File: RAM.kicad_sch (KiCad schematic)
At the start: 8 parts, among them U2 TXB0108DQSR, U3 TXB0108DQSR, U4 TXB0108DQSR, U5 74LVC1G04, U6 TXB0108DQSR, U7 AS6C1616, U8 TXB0108DQSR

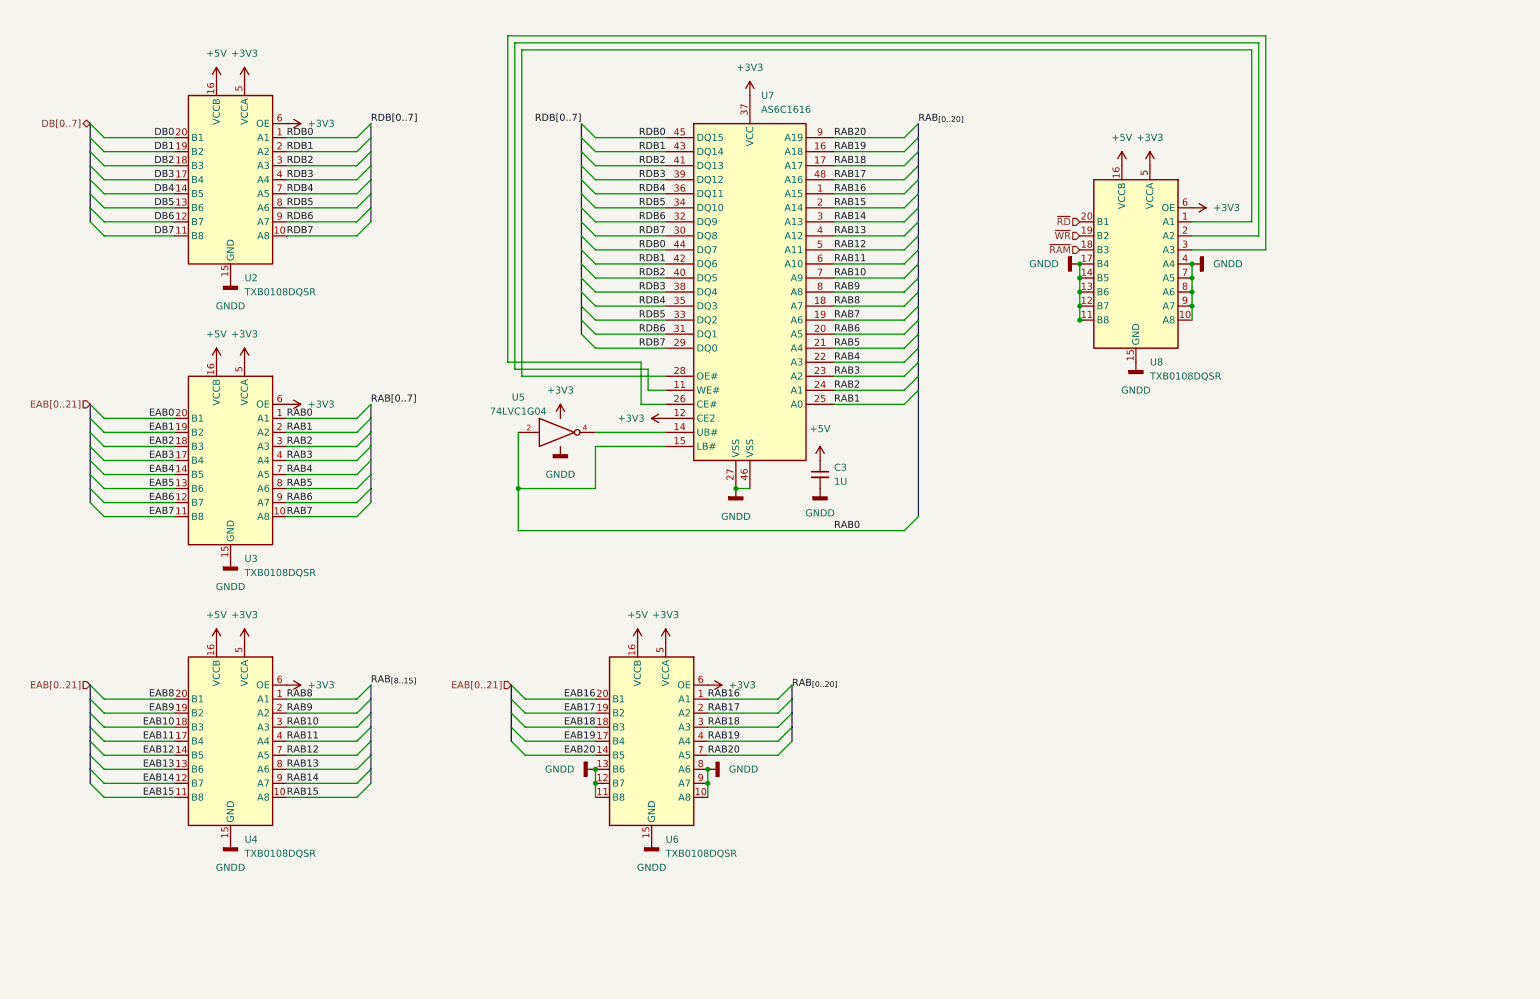
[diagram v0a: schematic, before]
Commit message: final hardware revision
final update to the hardware:
- removed flash
- added battery backup switch-over
- increased ram to 4MB
- added ramboot/netboot option by using reads to write-only ports to trigger/toggle
- fixed a logic bug i should have caught in writes to the mapper registers (using bits 14&15 instead of 1&0)
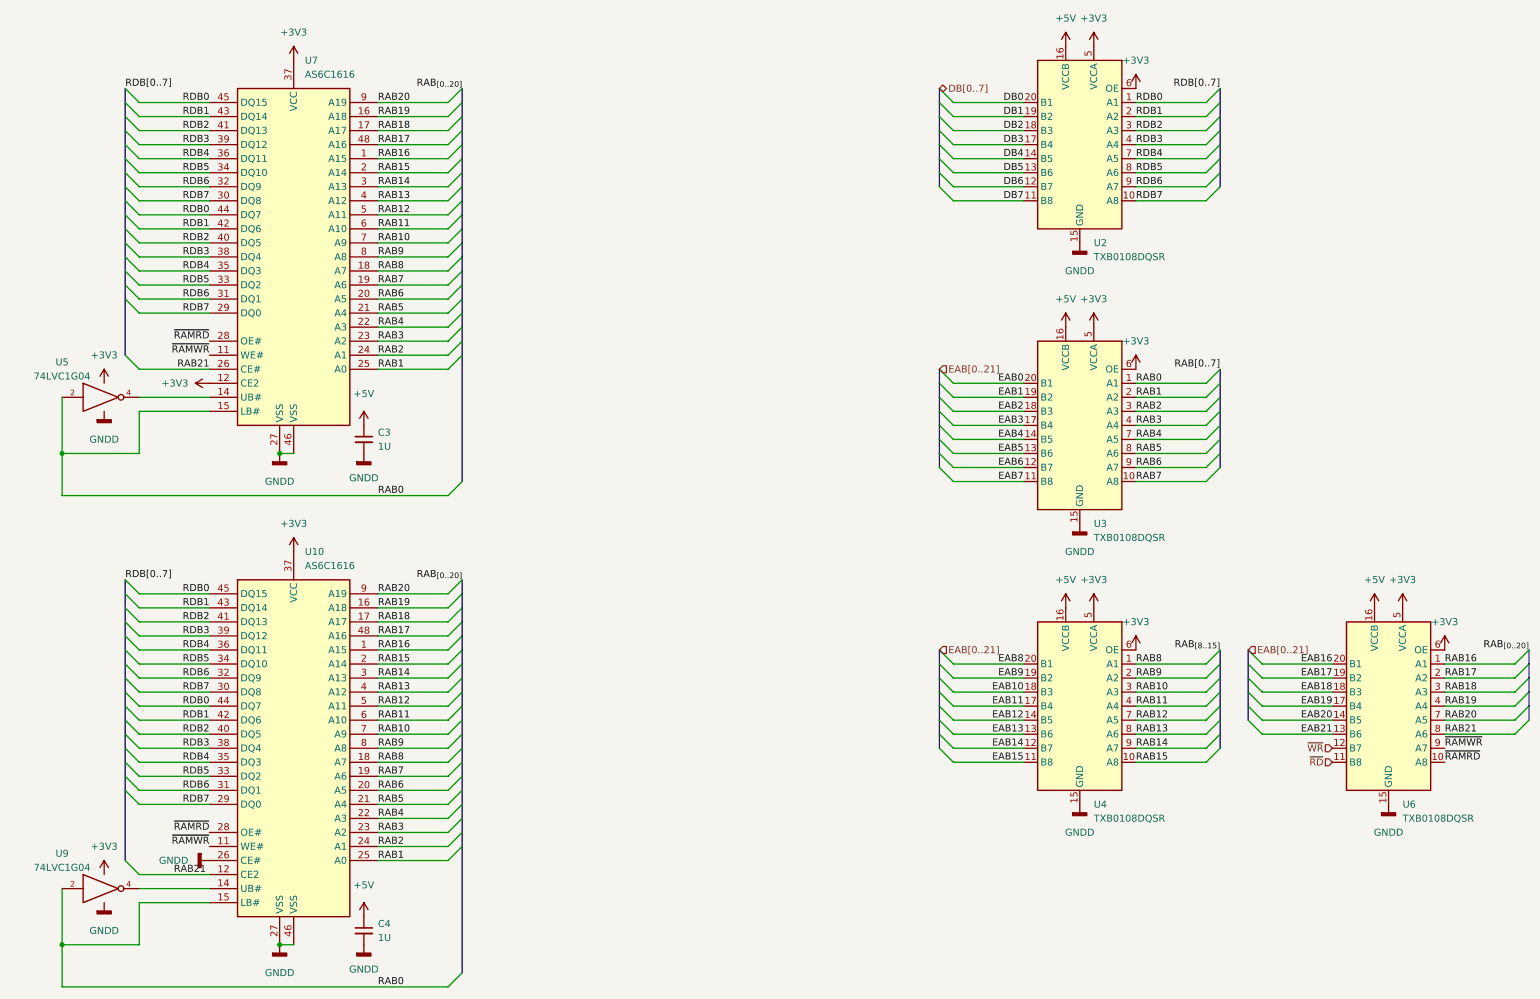
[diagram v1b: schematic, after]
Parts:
- removed U8: TXB0108DQSR, Package_SON:USON-20_2x4mm_P0.4mm, symbol Logic_LevelTranslator:TXB0108DQSR
- added C4: 1U, Capacitor_SMD:C_1206_3216Metric, symbol Device:C_Small
- added U10: AS6C1616, Package_SO:TSOP-I-48_18.4x12mm_P0.5mm, symbol Memory_RAM:AS6C1616
- added U9: 74LVC1G04, Package_TO_SOT_SMD:SOT-353_SC-70-5, symbol 74xGxx:74LVC1G04
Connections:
- net +3V3: now also U10.37 (VCC), U9.5 (VCC)
- net +5V: now also C4.1
- net GND: now also C4.2, U10.26 (CE#), U10.27 (VSS), U10.46 (VSS), U9.3 (GND); no longer U6.10 (A8), U6.11 (B8), U6.12 (B7), U6.13 (B6), U6.8 (A6), U6.9 (A7)
- net RAB0: now also U10.15 (LB#), U9.2
- net RAB1: now also U10.25 (A0)
- net RAB10: now also U10.7 (A9)
- net RAB11: now also U10.6 (A10)
- net RAB12: now also U10.5 (A11)
- net RAB13: now also U10.4 (A12)
- net RAB14: now also U10.3 (A13)
- net RAB15: now also U10.2 (A14)
- net RAB16: now also U10.1 (A15)
- net RAB17: now also U10.48 (A16)
- net RAB18: now also U10.17 (A17)
- net RAB19: now also U10.16 (A18)
- net RAB2: now also U10.24 (A1)
- net RAB20: now also U10.9 (A19)
- net RAB3: now also U10.23 (A2)
- net RAB4: now also U10.22 (A3)
- net RAB5: now also U10.21 (A4)
- net RAB6: now also U10.20 (A5)
- net RAB7: now also U10.19 (A6)
- net RAB8: now also U10.18 (A7)
- net RAB9: now also U10.8 (A8)
- net RDB0: now also U10.44 (DQ7), U10.45 (DQ15)
- net RDB1: now also U10.42 (DQ6), U10.43 (DQ14)
- net RDB2: now also U10.40 (DQ5), U10.41 (DQ13)
- net RDB3: now also U10.38 (DQ4), U10.39 (DQ12)
- net RDB4: now also U10.35 (DQ3), U10.36 (DQ11)
- net RDB5: now also U10.33 (DQ2), U10.34 (DQ10)
- net RDB6: now also U10.31 (DQ1), U10.32 (DQ9)
- net RDB7: now also U10.29 (DQ0), U10.30 (DQ8)
- net ~{RD}: now also U6.11 (B8)
- net ~{WR}: now also U6.12 (B7)
- net ~{RAMWR}: now reaches U7.11 (WE#)
- net ~{RAMWR}: now also U6.9 (A7), U10.11 (WE#)
- net RAB21: now reaches U7.26 (CE#)
- net RAB21: now also U6.8 (A6), U10.12 (CE2)
- net ~{RAMRD}: now reaches U7.28 (OE#)
- net ~{RAMRD}: now also U6.10 (A8), U10.28 (OE#)
- new net: U10.14 (UB#), U9.4
- new net EAB21: U6.13 (B6)
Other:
- moved on the sheet: C3, U2, U3, U4, U5, U6, U7
